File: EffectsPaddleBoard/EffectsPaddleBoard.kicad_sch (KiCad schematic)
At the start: 32 parts, among them J3 Barrel_Jack, U2 TPS7A0533PDBZ, U4 TPS54233, U5 TPS7A0533PDBZ, U8 TPS7A0518PDBZ

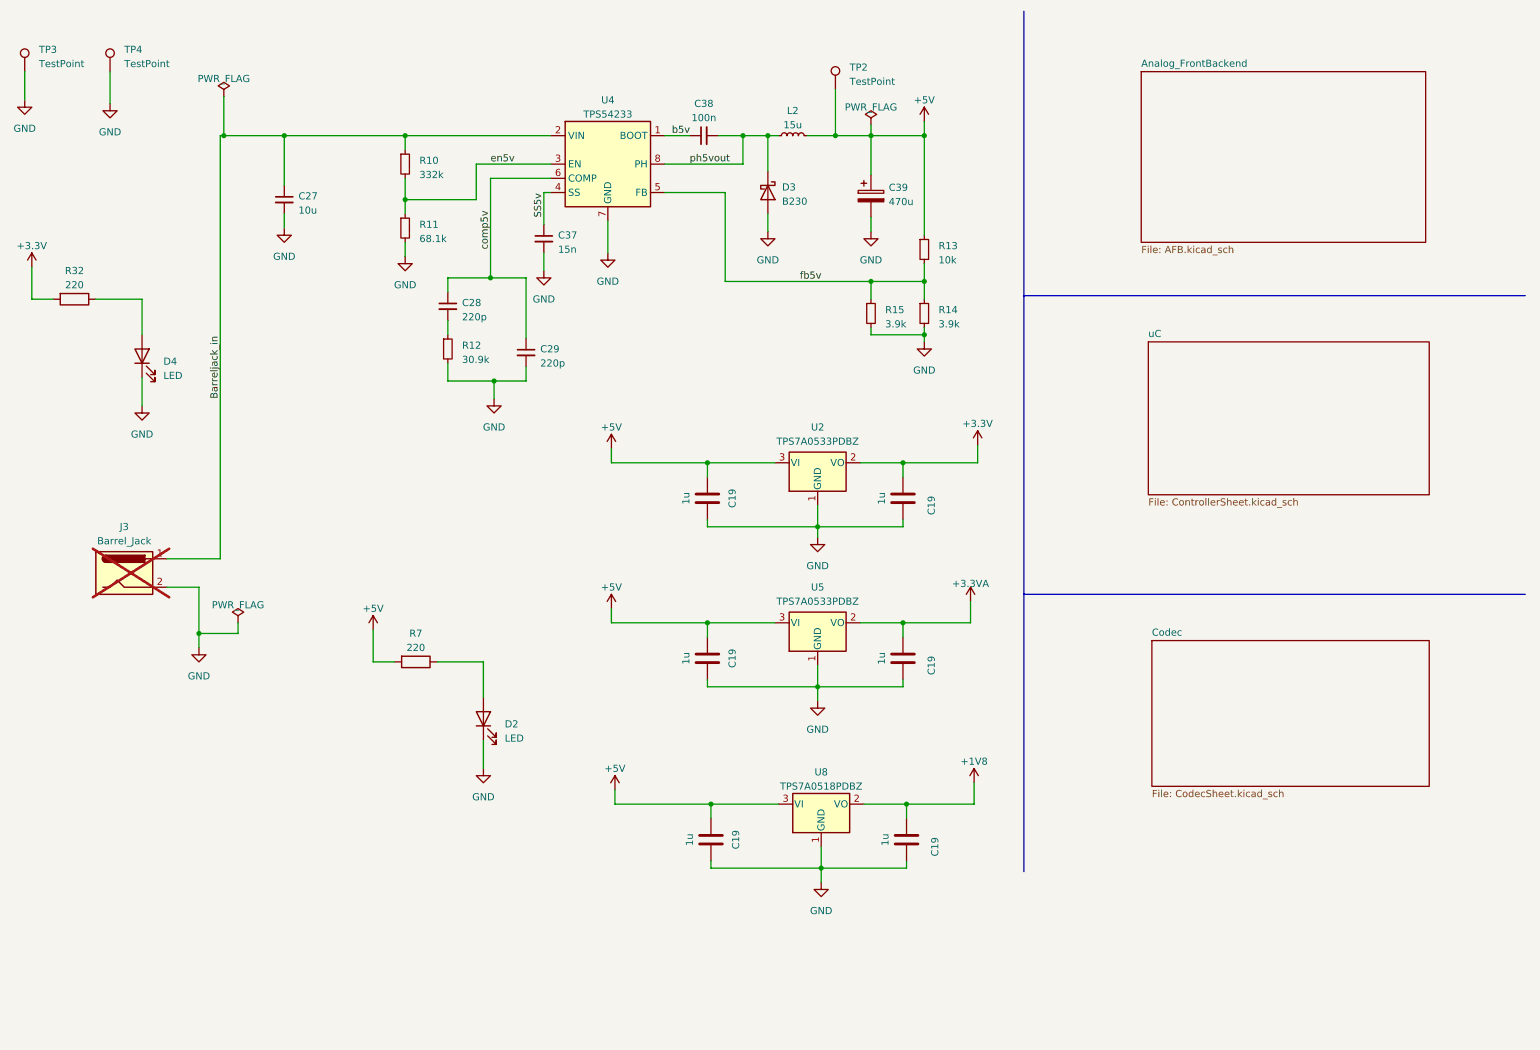
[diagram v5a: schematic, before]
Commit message: Added further testpoints
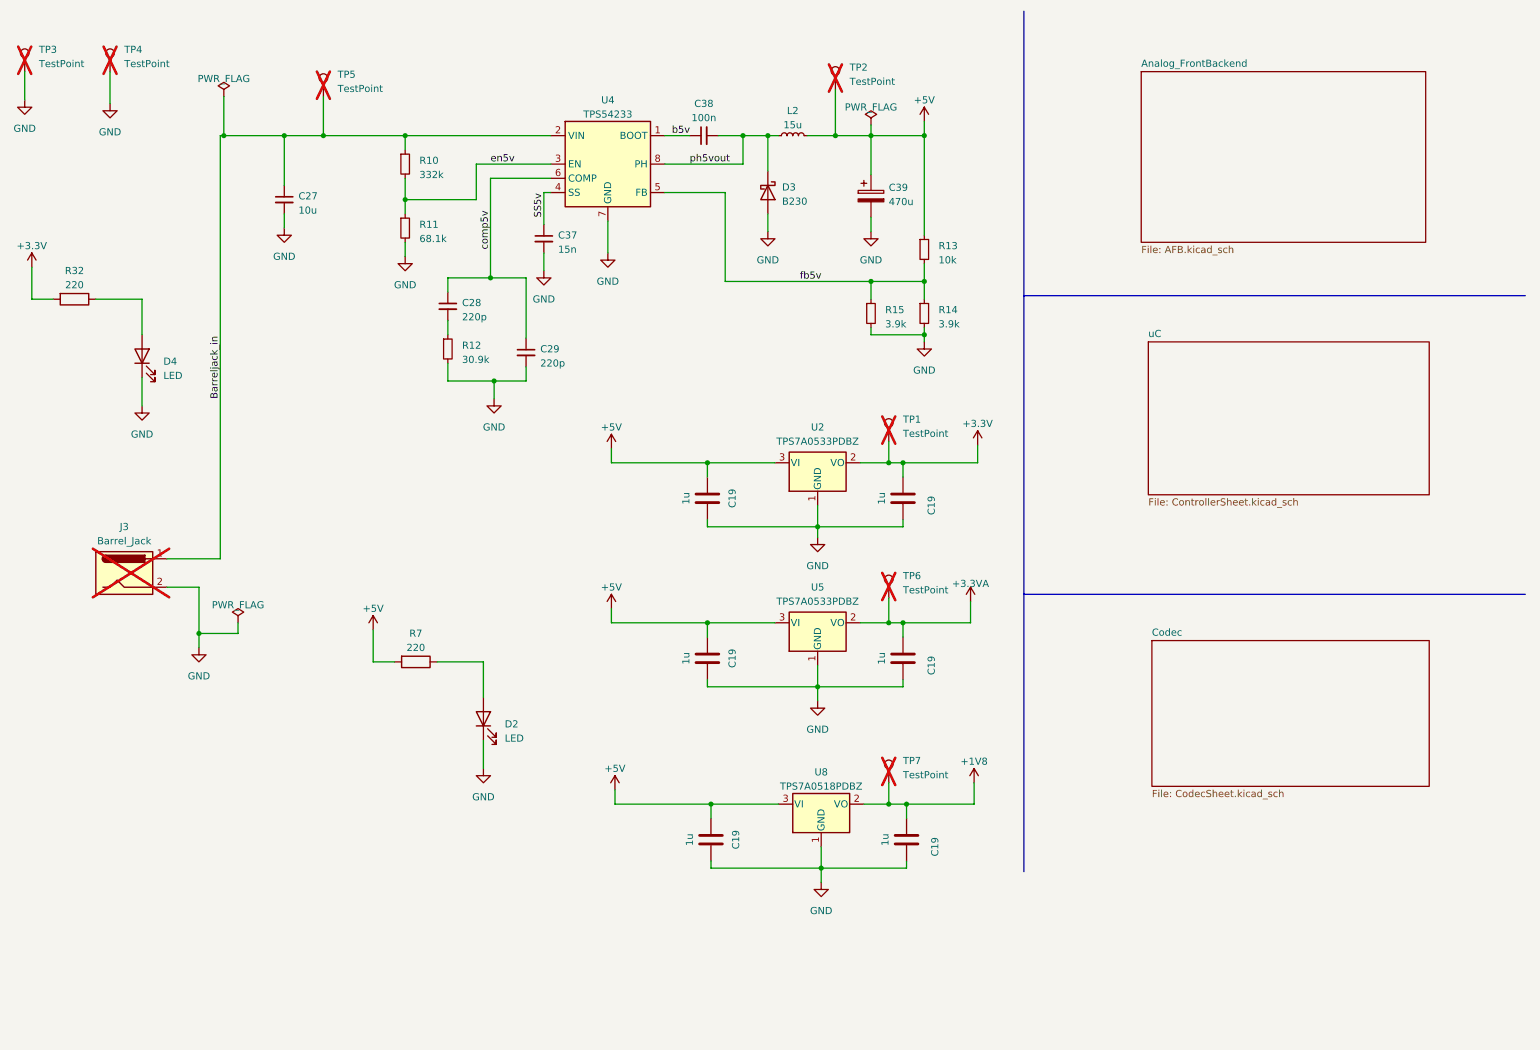
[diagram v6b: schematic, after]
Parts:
- added TP1, TP5, TP6, TP7: TestPoint, Connector_Pin:Pin_D1.3mm_L11.0mm, symbol Connector:TestPoint
- TP2, TP3, TP4: now not fitted; now left out of the parts list
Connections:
- net +1V8: now also TP7.1
- net +3.3V: now also TP1.1
- net +3.3VA: now also TP6.1
- net Barreljack_in: now also TP5.1
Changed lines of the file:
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@@
   (junction (at 100.965 78.105) (diameter 0) (color 0 0 0 0)
   )
+  (junction (at 171.45 153.67) (diameter 0) (color 0 0 0 0)
+  )
   (junction (at 174.625 153.67) (diameter 0) (color 0 0 0 0)
   )
+  (junction (at 70.485 34.29) (diameter 0) (color 0 0 0 0)
+  )
+  (junction (at 171.45 121.285) (diameter 0) (color 0 0 0 0)
+  )
   (junction (at 52.705 34.29) (diameter 0) (color 0 0 0 0)
   )
@@
   (junction (at 48.26 123.19) (diameter 0) (color 0 0 0 0)
   )
+  (junction (at 171.45 92.71) (diameter 0) (color 0 0 0 0)
+  )
   (junction (at 177.8 34.29) (diameter 0) (color 0 0 0 0)
   )
@@
     (stroke (width 0) (type default))
   )
+  (wire (pts (xy 171.45 153.67) (xy 174.625 153.67))
+    (stroke (width 0) (type default))
+  )
   (wire (pts (xy 161.925 26.035) (xy 161.925 34.29))
     (stroke (width 0) (type default))
@@
     (stroke (width 0) (type default))
   )
-  (wire (pts (xy 173.99 92.71) (xy 166.37 92.71))
+  (wire (pts (xy 173.99 92.71) (xy 171.45 92.71))
     (stroke (width 0) (type default))
   )
@@
     (stroke (width 0) (type default))
   )
+  (wire (pts (xy 70.485 27.305) (xy 70.485 34.29))
+    (stroke (width 0) (type default))
+  )
   (wire (pts (xy 100.33 41.91) (xy 100.33 59.69))
     (stroke (width 0) (type default))
@@
     (stroke (width 0) (type default))
   )
-  (wire (pts (xy 173.99 121.285) (xy 166.37 121.285))
+  (wire (pts (xy 173.99 121.285) (xy 171.45 121.285))
+    (stroke (width 0) (type default))
+  )
+  (wire (pts (xy 171.45 121.285) (xy 166.37 121.285))
     (stroke (width 0) (type default))
   )
@@
     (stroke (width 0) (type default))
   )
+  (wire (pts (xy 171.45 88.9) (xy 171.45 92.71))
+    (stroke (width 0) (type default))
+  )
   (wire (pts (xy 121.92 118.745) (xy 121.92 121.285))
     (stroke (width 0) (type default))
@@
     (stroke (width 0) (type default))
   )
+  (wire (pts (xy 171.45 92.71) (xy 166.37 92.71))
+    (stroke (width 0) (type default))
+  )
   (wire (pts (xy 99.06 128.27) (xy 99.06 134.62))
     (stroke (width 0) (type default))
@@
     (stroke (width 0) (type default))
   )
-  (wire (pts (xy 63.5 34.29) (xy 85.09 34.29))
+  (wire (pts (xy 63.5 34.29) (xy 70.485 34.29))
     (stroke (width 0) (type default))
   )
@@
     (stroke (width 0) (type default))
   )
+  (wire (pts (xy 171.45 149.86) (xy 171.45 153.67))
+    (stroke (width 0) (type default))
+  )
   (wire (pts (xy 177.8 68.58) (xy 177.8 69.85))
     (stroke (width 0) (type default))
@@
     (stroke (width 0) (type default))
   )
-  (wire (pts (xy 167.005 153.67) (xy 174.625 153.67))
+  (wire (pts (xy 167.005 153.67) (xy 171.45 153.67))
     (stroke (width 0) (type default))
   )
@@
     (stroke (width 0) (type default))
   )
+  (wire (pts (xy 70.485 34.29) (xy 85.09 34.29))
+    (stroke (width 0) (type default))
+  )
   (wire (pts (xy 187.325 89.535) (xy 187.325 92.71))
     (stroke (width 0) (type default))
@@
   )
   (wire (pts (xy 186.69 149.86) (xy 186.69 153.67))
+    (stroke (width 0) (type default))
+  )
+  (wire (pts (xy 171.45 116.84) (xy 171.45 121.285))
     (stroke (width 0) (type default))
   )
@@
   (label "b5v" (at 132.715 34.29 0) (fields_autoplaced)
     (effects (font (size 1.27 1.27)) (justify left bottom))
+  )
+  (symbol (lib_id "Connector:TestPoint") (at 171.45 149.86 0) (unit 1)
+    (in_bom no) (on_board yes) (dnp yes) (fields_autoplaced)
+    (property "Reference" "TP7" (at 173.99 145.923 0)
+      (effects (font (size 1.27 1.27)) (justify left))
+    )
+    (property "Value" "TestPoint" (at 173.99 148.463 0)
+      (effects (font (size 1.27 1.27)) (justify left))
+    )
+    (property "Footprint" "Connector_Pin:Pin_D1.3mm_L11.0mm" (at 176.53 149.86 0)
+      (effects (font (size 1.27 1.27)) hide)
+    )
+    (property "Datasheet" "~" (at 176.53 149.86 0)
+      (effects (font (size 1.27 1.27)) hide)
+    )
+    (property "Sim.Enable" "0" (at 171.45 149.86 0)
+      (effects (font (size 1.27 1.27)) hide)
+    )
+    (property "Distributer Link" "" (at 171.45 149.86 0)
+      (effects (font (size 1.27 1.27)) hide)
+    )
+    (property "Manufacturer" "" (at 171.45 149.86 0)
+      (effects (font (size 1.27 1.27)) hide)
+    )
+    (property "Manufacturer Part Number" "" (at 171.45 149.86 0)
+      (effects (font (size 1.27 1.27)) hide)
+    )
+    (pin "1")
+    (instances
+      (project "EffectsPaddleBoard"
+        (path "/40bb1606-5207-4492-95b9-876879aab2b4"
+          (reference "TP7") (unit 1)
+        )
+      )
+    )
   )
   (symbol (lib_id "Device:C_Small") (at 106.68 73.025 0) (unit 1)
@@
     )
   )
+  (symbol (lib_id "Connector:TestPoint") (at 70.485 27.305 0) (unit 1)
+    (in_bom no) (on_board yes) (dnp yes) (fields_autoplaced)
+    (property "Reference" "TP5" (at 73.025 23.368 0)
+      (effects (font (size 1.27 1.27)) (justify left))
+    )
+    (property "Value" "TestPoint" (at 73.025 25.908 0)
+      (effects (font (size 1.27 1.27)) (justify left))
+    )
+    (property "Footprint" "Connector_Pin:Pin_D1.3mm_L11.0mm" (at 75.565 27.305 0)
+      (effects (font (size 1.27 1.27)) hide)
+    )
+    (property "Datasheet" "~" (at 75.565 27.305 0)
+      (effects (font (size 1.27 1.27)) hide)
+    )
+    (property "Sim.Enable" "0" (at 70.485 27.305 0)
+      (effects (font (size 1.27 1.27)) hide)
+    )
+    (property "Distributer Link" "" (at 70.485 27.305 0)
+      (effects (font (size 1.27 1.27)) hide)
+    )
+    (property "Manufacturer" "" (at 70.485 27.305 0)
+      (effects (font (size 1.27 1.27)) hide)
+    )
+    (property "Manufacturer Part Number" "" (at 70.485 27.305 0)
+      (effects (font (size 1.27 1.27)) hide)
+    )
+    (pin "1")
+    (instances
+      (project "EffectsPaddleBoard"
+        (path "/40bb1606-5207-4492-95b9-876879aab2b4"
+          (reference "TP5") (unit 1)
+        )
+      )
+    )
+  )
   (symbol (lib_id "power:+5V") (at 122.555 151.13 0) (unit 1)
     (in_bom yes) (on_board yes) (dnp no) (fields_autoplaced)
@@
         (path "/40bb1606-5207-4492-95b9-876879aab2b4"
           (reference "#FLG03") (unit 1)
+        )
+      )
+    )
+  )
+  (symbol (lib_id "Connector:TestPoint") (at 171.45 116.84 0) (unit 1)
+    (in_bom no) (on_board yes) (dnp yes) (fields_autoplaced)
+    (property "Reference" "TP6" (at 173.99 112.903 0)
+      (effects (font (size 1.27 1.27)) (justify left))
+    )
+    (property "Value" "TestPoint" (at 173.99 115.443 0)
+      (effects (font (size 1.27 1.27)) (justify left))
+    )
+    (property "Footprint" "Connector_Pin:Pin_D1.3mm_L11.0mm" (at 176.53 116.84 0)
+      (effects (font (size 1.27 1.27)) hide)
+    )
+    (property "Datasheet" "~" (at 176.53 116.84 0)
+      (effects (font (size 1.27 1.27)) hide)
+    )
+    (property "Sim.Enable" "0" (at 171.45 116.84 0)
+      (effects (font (size 1.27 1.27)) hide)
+    )
+    (property "Distributer Link" "" (at 171.45 116.84 0)
+      (effects (font (size 1.27 1.27)) hide)
+    )
+    (property "Manufacturer" "" (at 171.45 116.84 0)
+      (effects (font (size 1.27 1.27)) hide)
+    )
+    (property "Manufacturer Part Number" "" (at 171.45 116.84 0)
+      (effects (font (size 1.27 1.27)) hide)
+    )
+    (pin "1")
+    (instances
+      (project "EffectsPaddleBoard"
+        (path "/40bb1606-5207-4492-95b9-876879aab2b4"
+          (reference "TP6") (unit 1)
         )
       )
@@
   )
   (symbol (lib_id "Connector:TestPoint") (at 161.925 26.035 0) (unit 1)
-    (in_bom yes) (on_board yes) (dnp no) (fields_autoplaced)
+    (in_bom no) (on_board yes) (dnp yes) (fields_autoplaced)
     (property "Reference" "TP2" (at 164.465 22.098 0)
       (effects (font (size 1.27 1.27)) (justify left))
@@
   )
   (symbol (lib_id "Connector:TestPoint") (at 32.385 22.86 0) (unit 1)
-    (in_bom yes) (on_board yes) (dnp no) (fields_autoplaced)
+    (in_bom no) (on_board yes) (dnp yes) (fields_autoplaced)
     (property "Reference" "TP4" (at 34.925 18.923 0)
       (effects (font (size 1.27 1.27)) (justify left))
@@
     )
   )
+  (symbol (lib_id "Connector:TestPoint") (at 171.45 88.9 0) (unit 1)
+    (in_bom no) (on_board yes) (dnp yes) (fields_autoplaced)
+    (property "Reference" "TP1" (at 173.99 84.963 0)
+      (effects (font (size 1.27 1.27)) (justify left))
+    )
+    (property "Value" "TestPoint" (at 173.99 87.503 0)
+      (effects (font (size 1.27 1.27)) (justify left))
+    )
+    (property "Footprint" "Connector_Pin:Pin_D1.3mm_L11.0mm" (at 176.53 88.9 0)
+      (effects (font (size 1.27 1.27)) hide)
+    )
+    (property "Datasheet" "~" (at 176.53 88.9 0)
+      (effects (font (size 1.27 1.27)) hide)
+    )
+    (property "Sim.Enable" "0" (at 171.45 88.9 0)
+      (effects (font (size 1.27 1.27)) hide)
+    )
+    (property "Distributer Link" "" (at 171.45 88.9 0)
+      (effects (font (size 1.27 1.27)) hide)
+    )
+    (property "Manufacturer" "" (at 171.45 88.9 0)
+      (effects (font (size 1.27 1.27)) hide)
+    )
+    (property "Manufacturer Part Number" "" (at 171.45 88.9 0)
+      (effects (font (size 1.27 1.27)) hide)
+    )
+    (pin "1")
+    (instances
+      (project "EffectsPaddleBoard"
+        (path "/40bb1606-5207-4492-95b9-876879aab2b4"
+          (reference "TP1") (unit 1)
+        )
+      )
+    )
+  )
   (symbol (lib_id "Regulator_Linear:TPS7A0533PDBZ") (at 158.75 92.71 0) (unit 1)
     (in_bom yes) (on_board yes) (dnp no) (fields_autoplaced)
@@
   )
   (symbol (lib_id "Connector:TestPoint") (at 17.145 22.86 0) (unit 1)
-    (in_bom yes) (on_board yes) (dnp no) (fields_autoplaced)
+    (in_bom no) (on_board yes) (dnp yes) (fields_autoplaced)
     (property "Reference" "TP3" (at 19.685 18.923 0)
       (effects (font (size 1.27 1.27)) (justify left))

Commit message: exported symbols and footprints, updated PCB
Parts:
- removed C27: 10u, Capacitor_SMD:C_0805_2012Metric, symbol Device:C_Small
- removed C28, C29: 220p, Capacitor_SMD:C_0402_1005Metric, symbol Device:C_Small
- removed C37: 15n, Capacitor_SMD:C_0402_1005Metric, symbol Device:C_Small
- removed C38: 100n, Capacitor_SMD:C_0402_1005Metric, symbol Device:C_Small
- removed C39: 470u, Capacitor_SMD:CP_Elec_8x10.5, symbol Device:C_Polarized
- removed D3: B230, Diode_SMD:D_SMB, symbol Diode:B230
- removed L2: 15u, Inductor_SMD:L_0805_2012Metric, symbol Device:L_Small
- removed R10: 332k, Resistor_SMD:R_1206_3216Metric, symbol Device:R_Small
- removed R11: 68.1k, Resistor_SMD:R_1206_3216Metric, symbol Device:R_Small
- removed R12: 30.9k, Resistor_SMD:R_1206_3216Metric, symbol Device:R_Small
- removed R13: 10k, Resistor_SMD:R_1206_3216Metric, symbol Device:R_Small
- removed R14, R15: 3.9k, Resistor_SMD:R_1206_3216Metric, symbol Device:R_Small
- removed U4: TPS54233, Package_SO:SOIC-8_3.9x4.9mm_P1.27mm, symbol Regulator_Switching:TPS54233
- added C1: 100n, Capacitor_SMD:C_0402_1005Metric, symbol EffectsPaddleBoard:C
- added C41, C42: 22u, Capacitor_SMD:C_0805_2012Metric, symbol EffectsPaddleBoard:C_Small
- added C47: 10u, Capacitor_SMD:C_0805_2012Metric, symbol EffectsPaddleBoard:C_Small
- added L1: 2.2u, Inductor_SMD:L_1210_3225Metric, symbol EffectsPaddleBoard:L_Small
- added R19: 10k, Resistor_SMD:R_0402_1005Metric, symbol EffectsPaddleBoard:R
- added R9: 52.3k, Resistor_SMD:R_0402_1005Metric, symbol EffectsPaddleBoard:R
- added U6: AP62250Z6, Package_TO_SOT_SMD:SOT-563, symbol EffectsPaddleBoard:AP62250Z6
- C19: symbol Device:C -> EffectsPaddleBoard:C
- D2, D4: symbol Device:LED -> EffectsPaddleBoard:LED
- J3: footprint Connector_BarrelJack:BarrelJack_SwitchcraftConxall_RAPC10U_Horizontal -> Library:BarrelJack_SwitchcraftConxall_RAPC10U_Horizontal; symbol Connector:Barrel_Jack -> EffectsPaddleBoard:Barrel_Jack
- R32, R7: symbol Device:R -> EffectsPaddleBoard:R
- TP1, TP2, TP3, TP4, TP5, TP6, TP7: symbol Connector:TestPoint -> EffectsPaddleBoard:TestPoint
- U2, U5: symbol Regulator_Linear:TPS7A0533PDBZ -> EffectsPaddleBoard:TPS7A0533PDBZ
- U8: symbol Regulator_Linear:TPS7A0518PDBZ -> EffectsPaddleBoard:TPS7A0518PDBZ
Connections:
- net +5V: now also C41.1, C42.1, L1.2, R9.1
- net Barreljack_in: now also C47.1, U6.1 (VIN)
- net GND: now also C41.2, C42.2, C47.2, R19.2, U6.3 (GND)
- new net v_bst: C1.2, U6.4 (BST)
- new net v_fb: R19.1, R9.2, U6.6 (FB)
- new net v_sw: C1.1, L1.1, U6.2 (SW)
- no-connect marks 0 -> 1
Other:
- note added: "floating EN: always acitve"
- moved on the sheet: C19, J3, R32, R7, TP2, TP3, TP4, TP5, U5, U8

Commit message: fixed manf part nr on inductor and caps
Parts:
- C41, C42: Manufacturer Part Number GCM21BC71E106KE36K -> GRM21BR61E226ME44L
- L1: Distributer Link (none) -> https://www.bourns.com/docs/product-datasheets/srp3212.pdf; Manufacturer (none) -> Bourns Inc.; Manufacturer Part Number (none) -> SRP3212-2R2M
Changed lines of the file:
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@@
       (effects (font (size 1.27 1.27)) hide)
     )
-    (property "Manufacturer Part Number" "GCM21BC71E106KE36K" (at 139.7 38.1 0)
+    (property "Manufacturer Part Number" "GRM21BR61E226ME44L" (at 139.7 38.1 0)
       (effects (font (size 1.27 1.27)) hide)
     )
@@
       (effects (font (size 1.27 1.27)) hide)
     )
-    (property "Manufacturer Part Number" "GCM21BC71E106KE36K" (at 130.81 38.1 0)
+    (property "Manufacturer Part Number" "GRM21BR61E226ME44L" (at 130.81 38.1 0)
       (effects (font (size 1.27 1.27)) hide)
     )
@@
       (effects (font (size 1.27 1.27)) hide)
     )
+    (property "Distributer Link" "https://www.bourns.com/docs/product-datasheets/srp3212.pdf" (at 124.46 34.29 0)
+      (effects (font (size 1.27 1.27)) hide)
+    )
+    (property "Manufacturer" "Bourns Inc." (at 124.46 34.29 0)
+      (effects (font (size 1.27 1.27)) hide)
+    )
+    (property "Manufacturer Part Number" "SRP3212-2R2M" (at 124.46 34.29 0)
+      (effects (font (size 1.27 1.27)) hide)
+    )
